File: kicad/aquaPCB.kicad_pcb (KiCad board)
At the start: 2 copper layers, 100 x 100 mm, 147 parts, among them J1 12V IN, J11 GPIO 17, J12 GPIO 22, J13 GPIO 23, J14 GPIO 27, J15 GPIO 5, J16 GPIO 6, J17 GPIO 20, J18 GPIO 21, J19 1-wire DS1820, J2 Raspberry Pi, J22 I2C 1, J23 I2C 2, J24 Display, J25 ADC #1 in 0, J26 ADC #1 in 2, J27 ADC #1 in 3, J4 PWM 0, J5 GPIO 12, J6 GPIO 13, J7 PWM 1, J8 GPIO 16, J9 GPIO 26, Q1 AOD4184A, Q10 AOD4185, Q2 AOD4184A, Q3 AOD4184A, Q4 AOD4184A, Q5 AOD4184A, Q6 AOD4184A, U1 TPS54360B, U2 AMS1117-3.3, U3 74HCT244D, U4 ULN2803A, U5 ADS1115IDGSR, U6 TLV9062IDR

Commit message: kicad: bottom-silk +3V3/GND marks for the inputs IN1..IN4 (J15..J18)
Co-Authored-By: Claude Opus 5.5 <noreply@anthropic.com>
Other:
- board text added: "+3V3"
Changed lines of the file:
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@@
+		)
+	)
+	(gr_text "+3V3"
+		(at 104.005 45.73 0)
+		(layer "B.SilkS")
+		(effects
+			(font
+				(size 0.8 0.8)
+				(thickness 0.15)
+			)
+			(justify mirror)
+		)
+	)
+	(gr_text "GND"
+		(at 111.005 45.73 0)
+		(layer "B.SilkS")
+		(effects
+			(font
+				(size 0.8 0.8)
+				(thickness 0.15)
+			)
+			(justify mirror)
 		)
 	)
 	(gr_text "GPIO 12"
 		(at 115.325 130.455 0)
+		(layer "B.SilkS")
+		(effects
+			(font
+				(size 0.8 0.8)
+				(thickness 0.15)
+			)
+			(justify mirror)
+		)
+	)
+	(gr_text "+3V3"
+		(at 117.205 45.73 0)
+		(layer "B.SilkS")
+		(effects
+			(font
+				(size 0.8 0.8)
+				(thickness 0.15)
+			)
+			(justify mirror)
+		)
+	)
+	(gr_text "GND"
+		(at 124.205 45.73 0)
 		(layer "B.SilkS")
 		(effects
@@
 		)
 	)
+	(gr_text "+3V3"
+		(at 130.404999 45.73 0)
+		(layer "B.SilkS")
+		(effects
+			(font
+				(size 0.8 0.8)
+				(thickness 0.15)
+			)
+			(justify mirror)
+		)
+	)
+	(gr_text "GND"
+		(at 137.404999 45.73 0)
+		(layer "B.SilkS")
+		(effects
+			(font
+				(size 0.8 0.8)
+				(thickness 0.15)
+			)
+			(justify mirror)
+		)
+	)
+	(gr_text "+3V3"
+		(at 143.605 45.73 0)
+		(layer "B.SilkS")
+		(effects
+			(font
+				(size 0.8 0.8)
+				(thickness 0.15)
+			)
+			(justify mirror)
+		)
+	)
 	(gr_text "GPIO 16"
 		(at 149.375 130.455 0)
 		(layer "B.SilkS")
 		(effects
+			(font
+				(size 0.8 0.8)
+				(thickness 0.15)
+			)
+			(justify mirror)
+		)
+	)
+	(gr_text "GND"
+		(at 150.605 45.73 0)
+		(layer "B.SilkS")
+		(effects

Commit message: kicad: voltage marks instead of "+" at J19 (+3V3), J26 (+5V), J27 (+3V3)
Co-Authored-By: Claude Opus 5.5 <noreply@anthropic.com>
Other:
- board text added: "+5V"
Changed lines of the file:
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@@
+		)
+	)
+	(gr_text "+3V3"
+		(at 89.905 57.67 0)
+		(layer "B.SilkS")
+		(effects
+			(font
+				(size 0.8 0.8)
+				(thickness 0.15)
+			)
+			(justify mirror)
+		)
+	)
+	(gr_text "+5V"
+		(at 90.805 45.73 0)
+		(layer "B.SilkS")
+		(effects
+			(font
+				(size 0.8 0.8)
+				(thickness 0.15)
+			)
+			(justify mirror)
 		)
 	)
@@
 	(gr_text "GND"
 		(at 173.344999 47.33 90)
+		(layer "B.SilkS")
+		(effects
+			(font
+				(size 0.8 0.8)
+				(thickness 0.15)
+			)
+			(justify mirror)
+		)
+	)
+	(gr_text "+3V3"
+		(at 173.344999 54.33 90)
 		(layer "B.SilkS")
 		(effects
@@
 	)
 	(gr_text "+"
-		(at 89.105 57.67 0)
-		(layer "B.SilkS")
-		(effects
-			(font
-				(size 1.2 1.2)
-				(thickness 0.2)
-			)
-			(justify mirror)
-		)
-	)
-	(gr_text "+"
-		(at 90.805 46.029999 0)
-		(layer "B.SilkS")
-		(effects
-			(font
-				(size 1.2 1.2)
-				(thickness 0.2)
-			)
-			(justify mirror)
-		)
-	)
-	(gr_text "+"
 		(at 107.725 130.454999 0)
 		(layer "B.SilkS")
@@
 		(layer "B.SilkS")
 		(effects
-			(font
-				(size 1.2 1.2)
-				(thickness 0.2)
-			)
-			(justify mirror)
-		)
-	)
-	(gr_text "+"
-		(at 173.344999 54.33 0)
-		(layer "B.SilkS")
-		(effects

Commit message: kicad: I2C pin names (GND/3V3/SCL/SDA) on the bottom silk between J22 and J23
Co-Authored-By: Claude Opus 5.5 <noreply@anthropic.com>
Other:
- board text added: "3V3"
- board text added: "SCL"
- board text added: "SDA"
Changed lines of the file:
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@@
+	)
+	(gr_text "GND"
+		(at 157.35 37.595 90)
+		(layer "B.SilkS")
+		(effects
+			(font
+				(size 0.8 0.8)
+				(thickness 0.15)
+			)
+			(justify mirror)
+		)
+	)
+	(gr_text "3V3"
+		(at 157.35 40.135 90)
+		(layer "B.SilkS")
+		(effects
+			(font
+				(size 0.8 0.8)
+				(thickness 0.15)
+			)
+			(justify mirror)
+		)
+	)
+	(gr_text "SCL"
+		(at 157.35 42.675 90)
+		(layer "B.SilkS")
+		(effects
+			(font
+				(size 0.8 0.8)
+				(thickness 0.15)
+			)
+			(justify mirror)
+		)
+	)
+	(gr_text "SDA"
+		(at 157.35 45.215 90)
+		(layer "B.SilkS")
+		(effects
+			(font
+				(size 0.8 0.8)
+				(thickness 0.15)
+			)
+			(justify mirror)
+		)
 	)
 	(gr_text "GND"

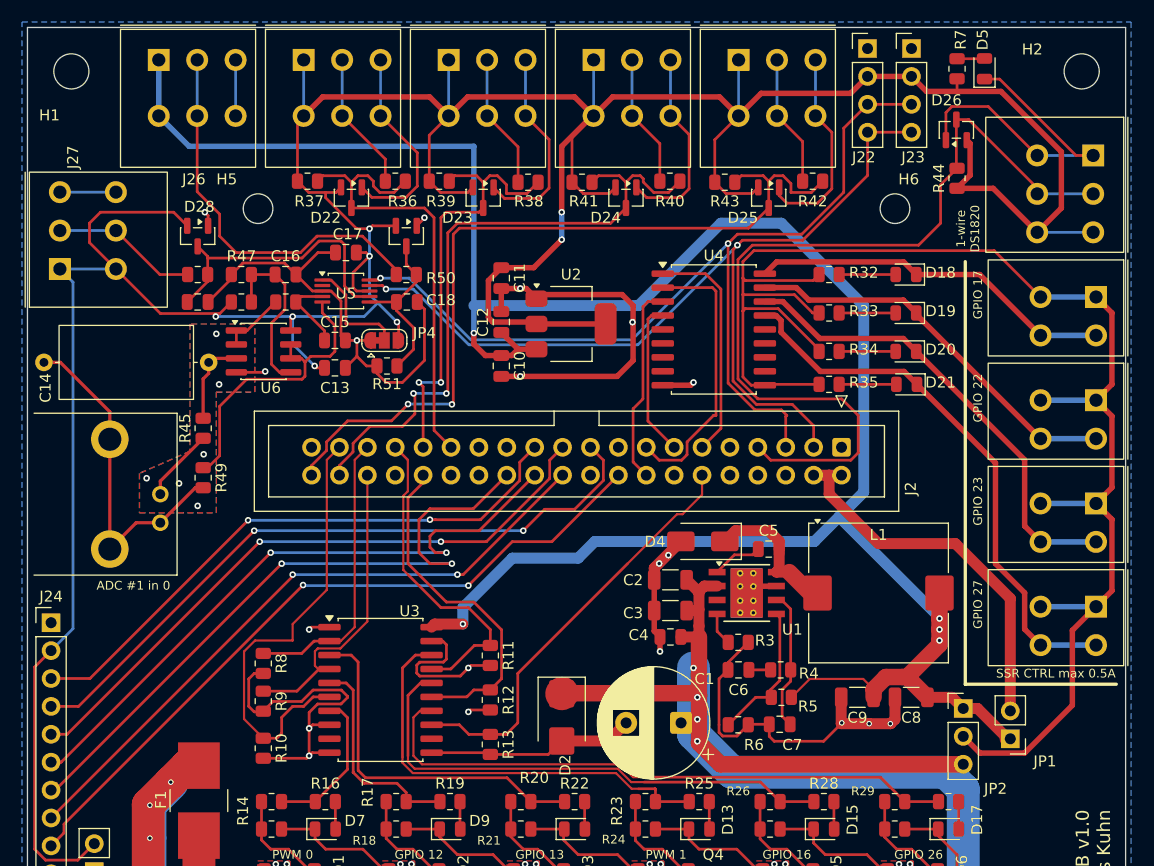
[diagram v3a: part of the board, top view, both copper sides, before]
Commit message: kicad: strip obsolete v1 parts for v2 (SSR sheet, IN1..IN4, pH front end)
41 parts, their tracks/vias, pH guard zones, BNC keep-out and port silk removed; freed J2/U5 pins marked no-connect. ERC 0, DRC 0, parity 0; one expected +3V3 ratsnest to J24/JP3/J27/D28 left for the v2 layout.

Co-Authored-By: Claude Opus 5.5 <noreply@anthropic.com>
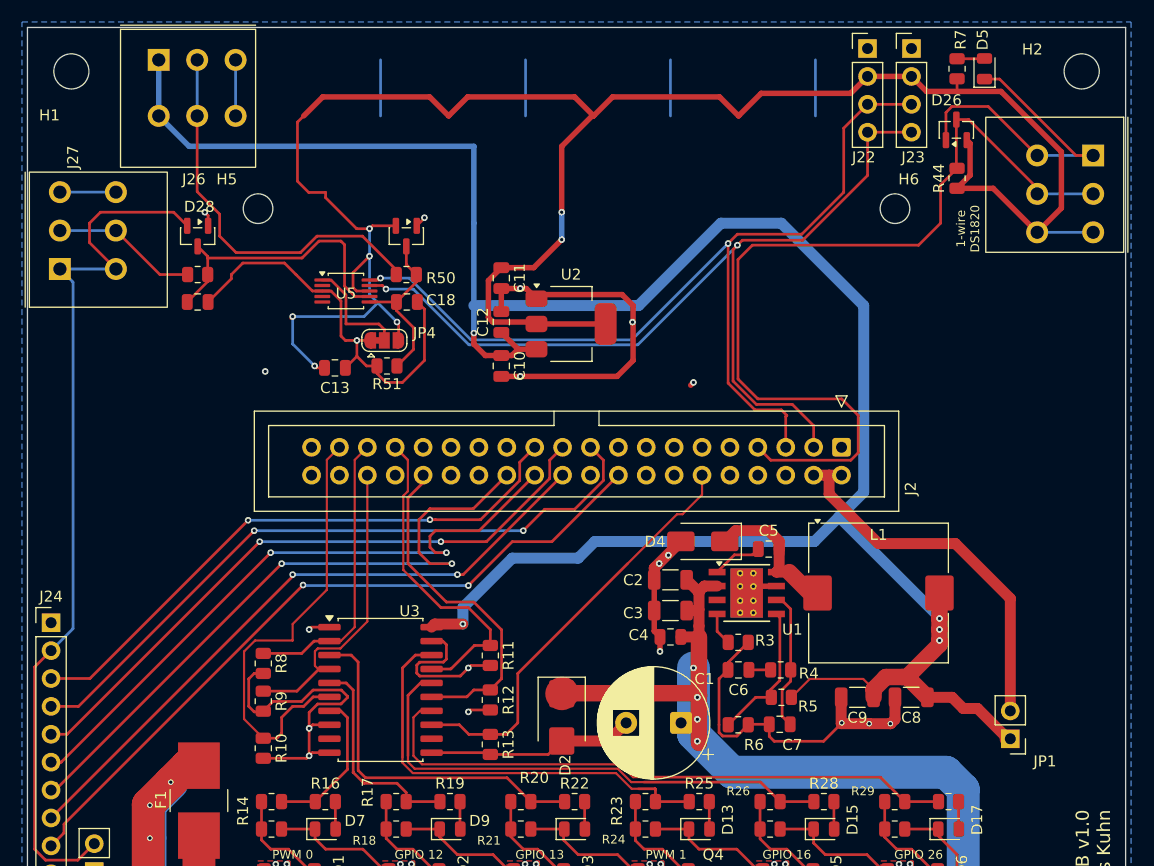
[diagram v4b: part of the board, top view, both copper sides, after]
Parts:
- removed C14: 6n8 styroflex, Capacitor_THT:C_Axial_L12.0mm_D6.5mm_P15.00mm_Horizontal
- removed C15: 10u, Capacitor_SMD:C_0805_2012Metric
- removed C16, C17: 100n, Capacitor_SMD:C_0805_2012Metric
- removed D18: GPIO17, LED_SMD:LED_0805_2012Metric
- removed D19: GPIO22, LED_SMD:LED_0805_2012Metric
- removed D20: GPIO23, LED_SMD:LED_0805_2012Metric
- removed D21: GPIO27, LED_SMD:LED_0805_2012Metric
- removed D22, D23, D24, D25: BAT54S, Package_TO_SOT_SMD:SOT-23
- removed J11: GPIO 17, aquaPCB:TerminalBlock_Kangnex_WJ250B-3.5-02P_P3.50mm_Staggered
- removed J12: GPIO 22, aquaPCB:TerminalBlock_Kangnex_WJ250B-3.5-02P_P3.50mm_Staggered
- removed J13: GPIO 23, aquaPCB:TerminalBlock_Kangnex_WJ250B-3.5-02P_P3.50mm_Staggered
- removed J14: GPIO 27, aquaPCB:TerminalBlock_Kangnex_WJ250B-3.5-02P_P3.50mm_Staggered
- removed J15: GPIO 5, aquaPCB:TerminalBlock_Kangnex_WJ250B-3.5-03P_P3.50mm_Staggered
- removed J16: GPIO 6, aquaPCB:TerminalBlock_Kangnex_WJ250B-3.5-03P_P3.50mm_Staggered
- removed J17: GPIO 20, aquaPCB:TerminalBlock_Kangnex_WJ250B-3.5-03P_P3.50mm_Staggered
- removed J18: GPIO 21, aquaPCB:TerminalBlock_Kangnex_WJ250B-3.5-03P_P3.50mm_Staggered
- removed J25: ADC #1 in 0, aquaPCB:BNC_HanElectricity_BNC-Q9-50KWE_Horizontal
- removed JP2: SSR supply, Connector_PinHeader_2.54mm:PinHeader_1x03_P2.54mm_Vertical
- removed R32, R33, R34, R35: 4k7, Resistor_SMD:R_0805_2012Metric
- removed R36, R38, R40, R42: 1k, Resistor_SMD:R_0805_2012Metric
- removed R37, R39, R41, R43, R46, R47, R48: 10k, Resistor_SMD:R_0805_2012Metric
- removed R45: 10M, Resistor_SMD:R_0805_2012Metric
- removed R49: 1M, Resistor_SMD:R_0805_2012Metric
- removed U4: ULN2803A, Package_SO:SOIC-18W_7.5x11.6mm_P1.27mm
- removed U6: TLV9062IDR, Package_SO:SOIC-8_3.9x4.9mm_P1.27mm
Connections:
- J2 pad 11: GPIO17_S1 -> unconnected-(J2-Pin_11-Pad11)
- J2 pad 13: GPIO27_S4 -> unconnected-(J2-Pin_13-Pad13)
- J2 pad 15: GPIO22_S2 -> unconnected-(J2-Pin_15-Pad15)
- J2 pad 16: GPIO23_S3 -> unconnected-(J2-Pin_16-Pad16)
- J2 pad 29: GPIO5_IN1 -> unconnected-(J2-Pin_29-Pad29)
- J2 pad 31: GPIO6_IN2 -> unconnected-(J2-Pin_31-Pad31)
- J2 pad 38: GPIO20_IN3 -> unconnected-(J2-Pin_38-Pad38)
- J2 pad 40: GPIO21_IN4 -> unconnected-(J2-Pin_40-Pad40)
- U5 pad 4: /ADS1115 ADC and pH amplifier/PH_SIG -> unconnected-(U5-AIN0-Pad4)
- U5 pad 5: /ADS1115 ADC and pH amplifier/PH_REF -> unconnected-(U5-AIN1-Pad5)
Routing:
- net /SSR / relay control outputs S1..S4/SSR_V: track 144.9 -> 0.00 mm
- net +3V3: track 349.7 -> 271.0 mm, vias 8 -> 7
- net GPIO21_IN4: track 74.3 -> 0.00 mm, vias 2 -> 0
- net GND: track 390.2 -> 327.2 mm
- net GPIO20_IN3: track 59.2 -> 0.00 mm, vias 2 -> 0
- net /SSR / relay control outputs S1..S4/S4_OUT: track 50.5 -> 0.00 mm
- net /SSR / relay control outputs S1..S4/S3_OUT: track 42.8 -> 0.00 mm
- net GPIO5_IN1: track 41.8 -> 0.00 mm
- net GPIO6_IN2: track 40.0 -> 0.00 mm, vias 2 -> 0
- net /SSR / relay control outputs S1..S4/S2_OUT: track 35.9 -> 0.00 mm
- net /SSR / relay control outputs S1..S4/S1_OUT: track 33.4 -> 0.00 mm
- net Net-(J25-Ext): track 31.2 -> 0.00 mm
- net /ADS1115 ADC and pH amplifier/PH_REF: track 27.5 -> 0.00 mm
- net GPIO22_S2: track 25.5 -> 0.00 mm
- net VIN: track 369.6 -> 344.7 mm
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- removed copper zone on B.Cu, net /ADS1115 ADC and pH amplifier/PH_BUF
- removed copper zone on F.Cu, net /ADS1115 ADC and pH amplifier/PH_BUF
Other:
- board text removed: "ADC #1 in 0"
- board text removed: "GPIO 17"
- board text removed: "GPIO 20"
- board text removed: "GPIO 21"
- board text removed: "GPIO 22"
- board text removed: "GPIO 23"
- board text removed: "GPIO 27"
- board text removed: "GPIO 5"
- board text removed: "GPIO 6"
- board text removed: "SSR CTRL max 0.5A"

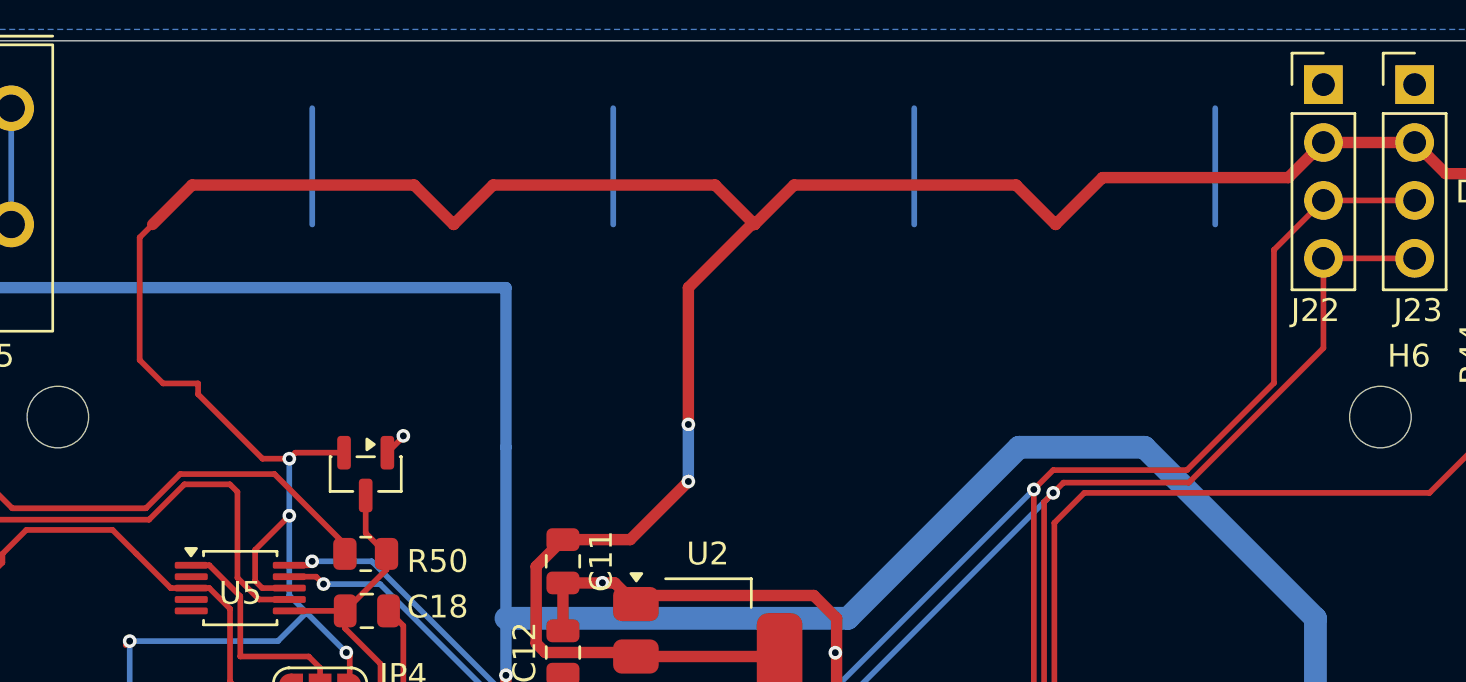
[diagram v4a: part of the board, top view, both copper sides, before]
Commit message: kicad: remove +3V3 routing for the v2 re-layout
Change made by hand in pcbnew (25 tracks, 2 vias on +3V3); committed on request before the v2 schematic work.

Co-Authored-By: Claude Opus 5.5 <noreply@anthropic.com>
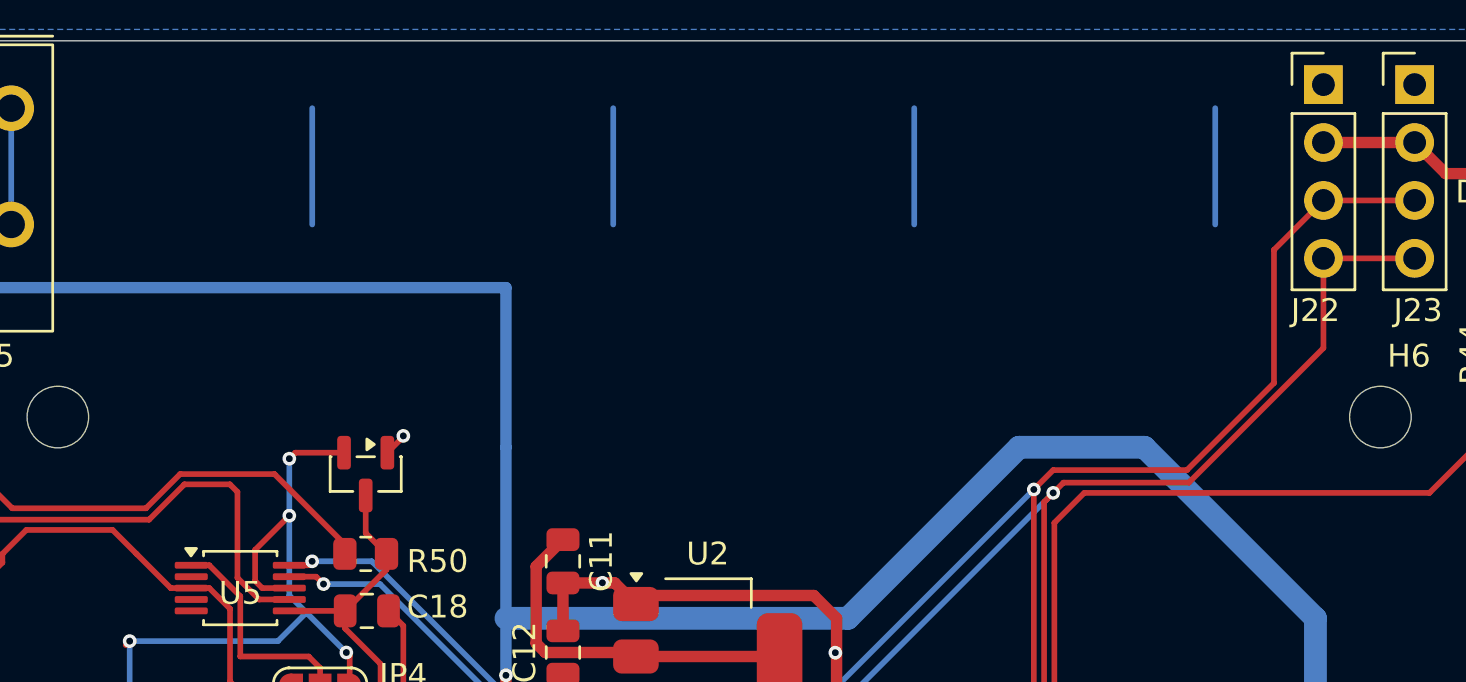
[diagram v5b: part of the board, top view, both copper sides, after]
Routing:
- net +3V3: track 271.0 -> 179.9 mm, vias 7 -> 5
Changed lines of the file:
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@@
 	)
 	(segment
-		(start 130.27 43.73)
-		(end 127.5 46.5)
-		(width 0.5)
-		(layer "F.Cu")
-		(net "+3V3")
-	)
-	(segment
 		(start 108.5 59.363604)
 		(end 108.811396 59.675)
@@
 	)
 	(segment
-		(start 141.875 42)
-		(end 132.134999 42)
-		(width 0.5)
-		(layer "F.Cu")
-		(net "+3V3")
-	)
-	(segment
 		(start 120.825 62.096878)
 		(end 120.825 58.725)
@@
 	)
 	(segment
-		(start 122 57.55)
-		(end 124.95 57.55)
-		(width 0.5)
-		(layer "F.Cu")
-		(net "+3V3")
-	)
-	(segment
-		(start 143.605 43.73)
-		(end 141.875 42)
-		(width 0.5)
-		(layer "F.Cu")
-		(net "+3V3")
-	)
-	(segment
-		(start 128.674999 42)
-		(end 118.935 42)
-		(width 0.5)
-		(layer "F.Cu")
-		(net "+3V3")
-	)
-	(segment
 		(start 79.5 110.5)
 		(end 79.5 93.92)
@@
 	)
 	(segment
-		(start 105.735 42)
-		(end 104.005 43.73)
-		(width 0.5)
-		(layer "F.Cu")
-		(net "+3V3")
-	)
-	(segment
-		(start 118.935 42)
-		(end 117.205 43.73)
-		(width 0.5)
-		(layer "F.Cu")
-		(net "+3V3")
-	)
-	(segment
 		(start 79.5 93.92)
 		(end 81 92.42)
@@
 	)
 	(segment
-		(start 106 50.7)
-		(end 106 51.175908)
-		(width 0.25)
-		(layer "F.Cu")
-		(net "+3V3")
-	)
-	(segment
 		(start 170.794999 54.33)
 		(end 166.789999 50.325)
@@
 	)
 	(segment
-		(start 130.404999 43.73)
-		(end 130.27 43.73)
-		(width 0.5)
-		(layer "F.Cu")
-		(net "+3V3")
-	)
-	(segment
-		(start 132.134999 42)
-		(end 130.404999 43.73)
-		(width 0.5)
-		(layer "F.Cu")
-		(net "+3V3")
-	)
-	(segment
 		(start 125.025 62.5)
 		(end 121.228122 62.5)
@@
 	)
 	(segment
-		(start 106 50.7)
-		(end 104.4625 50.7)
-		(width 0.25)
-		(layer "F.Cu")
-		(net "+3V3")
-	)
-	(segment
 		(start 85.5 52.5)
 		(end 84.5 53.5)
@@
 	)
 	(segment
-		(start 124.95 57.55)
-		(end 127.5 55)
-		(width 0.5)
-		(layer "F.Cu")
-		(net "+3V3")
-	)
-	(segment
 		(start 93.4 53.7375)
 		(end 92.1625 52.5)
@@
 	)
 	(segment
-		(start 115.475 42)
-		(end 105.735 42)
-		(width 0.5)
-		(layer "F.Cu")
-		(net "+3V3")
-	)
-	(segment
 		(start 159.35 40.135)
 		(end 160.715 41.5)
@@
 	)
 	(segment
-		(start 103.4375 44.2975)
-		(end 104.005 43.73)
-		(width 0.25)
-		(layer "F.Cu")
-		(net "+3V3")
-	)
-	(segment
-		(start 106 51.175908)
-		(end 108.824092 54)
-		(width 0.25)
-		(layer "F.Cu")
-		(net "+3V3")
-	)
-	(segment
-		(start 103.4375 49.675)
-		(end 103.4375 44.2975)
-		(width 0.25)
-		(layer "F.Cu")
-		(net "+3V3")
-	)
-	(segment
-		(start 143.605 43.73)
-		(end 145.66 41.675)
-		(width 0.5)
-		(layer "F.Cu")
-		(net "+3V3")
-	)
-	(segment
 		(start 163.5 40.35)
 		(end 163.5 41.5)
@@
 	)
 	(segment
-		(start 104.4625 50.7)
-		(end 103.4375 49.675)
-		(width 0.25)
-		(layer "F.Cu")
-		(net "+3V3")
-	)
-	(segment
-		(start 127.5 46.5)
-		(end 127.5 52.5)
-		(width 0.5)
-		(layer "F.Cu")
-		(net "+3V3")
-	)
-	(segment
 		(start 84.5 53.5)
 		(end 84.5 55.265)
@@
 	)
 	(segment
-		(start 108.824092 54)
-		(end 110 54)
-		(width 0.25)
-		(layer "F.Cu")
-		(net "+3V3")
-	)
-	(segment
-		(start 130.404999 43.73)
-		(end 128.674999 42)
-		(width 0.5)
-		(layer "F.Cu")
-		(net "+3V3")
-	)
-	(segment
 		(start 164.6875 46.2375)
 		(end 164.3875 45.9375)
@@
 	)
 	(segment
-		(start 117.205 43.73)
-		(end 115.475 42)
-		(width 0.5)
-		(layer "F.Cu")
-		(net "+3V3")
-	)
-	(segment
 		(start 164.6875 49.1375)
 		(end 164.6875 46.2375)
@@
 	)
 	(segment
-		(start 145.66 41.675)
-		(end 153.81 41.675)
-		(width 0.5)
-		(layer "F.Cu")
-		(net "+3V3")
-	)
-	(segment
 		(start 105.175 66.675)
 		(end 105 66.5)
@@
 	)
 	(segment
-		(start 153.81 41.675)
-		(end 155.35 40.135)
-		(width 0.5)
-		(layer "F.Cu")
-		(net "+3V3")
-	)
-	(segment
 		(start 92.1625 52.5)
 		(end 85.5 52.5)
@@
 	)
 	(via
-		(at 127.5 52.5)
-		(size 0.6)
-		(drill 0.3)
-		(layers "F.Cu" "B.Cu")
-		(net "+3V3")
-	)
-	(via
 		(at 110 56.5)
 		(size 0.6)
@@
 	)
 	(via
-		(at 127.5 55)
-		(size 0.6)
-		(drill 0.3)
-		(layers "F.Cu" "B.Cu")
-		(net "+3V3")
-	)
-	(via
 		(at 105 66.5)
 		(size 0.6)
@@
 	)
 	(segment
-		(start 127.5 55)
-		(end 127.5 52.5)
-		(width 0.5)
-		(layer "B.Cu")
-		(net "+3V3")
-	)
-	(segment
 		(start 112.5 62.5)
 		(end 110.75 60.75)
@@
 		)
 		(min_thickness 0.25)
-		(fill yes
+		(fill
 			(thermal_gap 0.5)
 			(thermal_bridge_width 0.5)
@@
 		)
 		(min_thickness 0.25)
-		(fill yes
+		(fill
 			(thermal_gap 0.5)
 			(thermal_bridge_width 0.5)
@@
 		)
 		(min_thickness 0.25)
-		(fill yes
+		(fill
 			(thermal_gap 0.5)
 			(thermal_bridge_width 0.5)
@@
 		)
 		(min_thickness 0.25)
-		(fill yes
+		(fill
 			(thermal_gap 0.5)
 			(thermal_bridge_width 0.5)
@@
 		)
 		(min_thickness 0.25)
-		(fill yes
+		(fill
 			(thermal_gap 0.5)
 			(thermal_bridge_width 0.5)
@@
 		)
 		(min_thickness 0.25)
-		(fill yes
+		(fill
 			(thermal_gap 0.5)
 			(thermal_bridge_width 0.5)
@@
 		)
 		(min_thickness 0.25)
-		(fill yes
+		(fill
 			(thermal_gap 0.5)
 			(thermal_bridge_width 0.5)
